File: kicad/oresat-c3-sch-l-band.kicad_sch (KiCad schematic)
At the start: 82 parts, among them U15 Qorvo 856930, U16 AX5043, U17 SI4112, U2 BP0805A1308, U29 TQP3M9036, U3 BP0805A1308, U4 BGB741L7ESD, U5 BP0805A1308, U7 MAC-24+

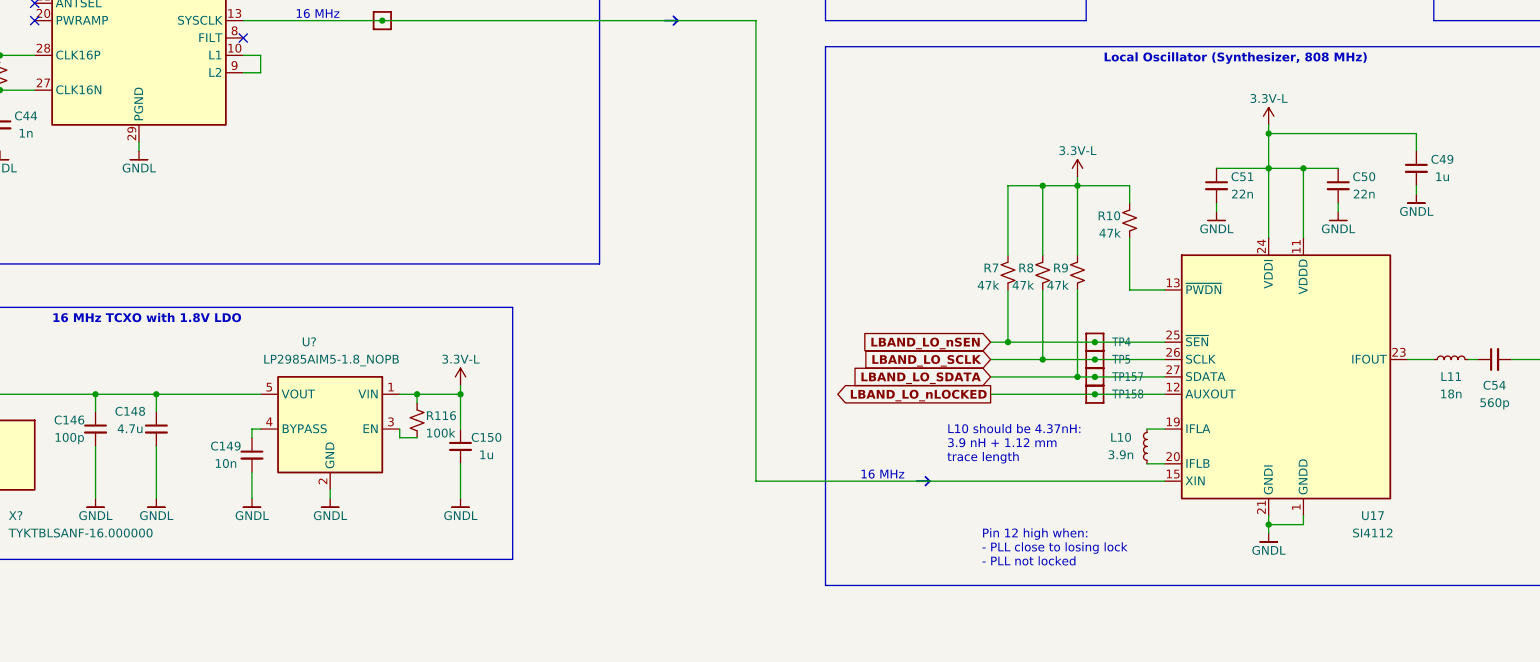
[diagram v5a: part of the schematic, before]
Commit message: More progress on C3 v6. All ICs and Packages are in, deployer and power supply and I2C subsystems laid out.
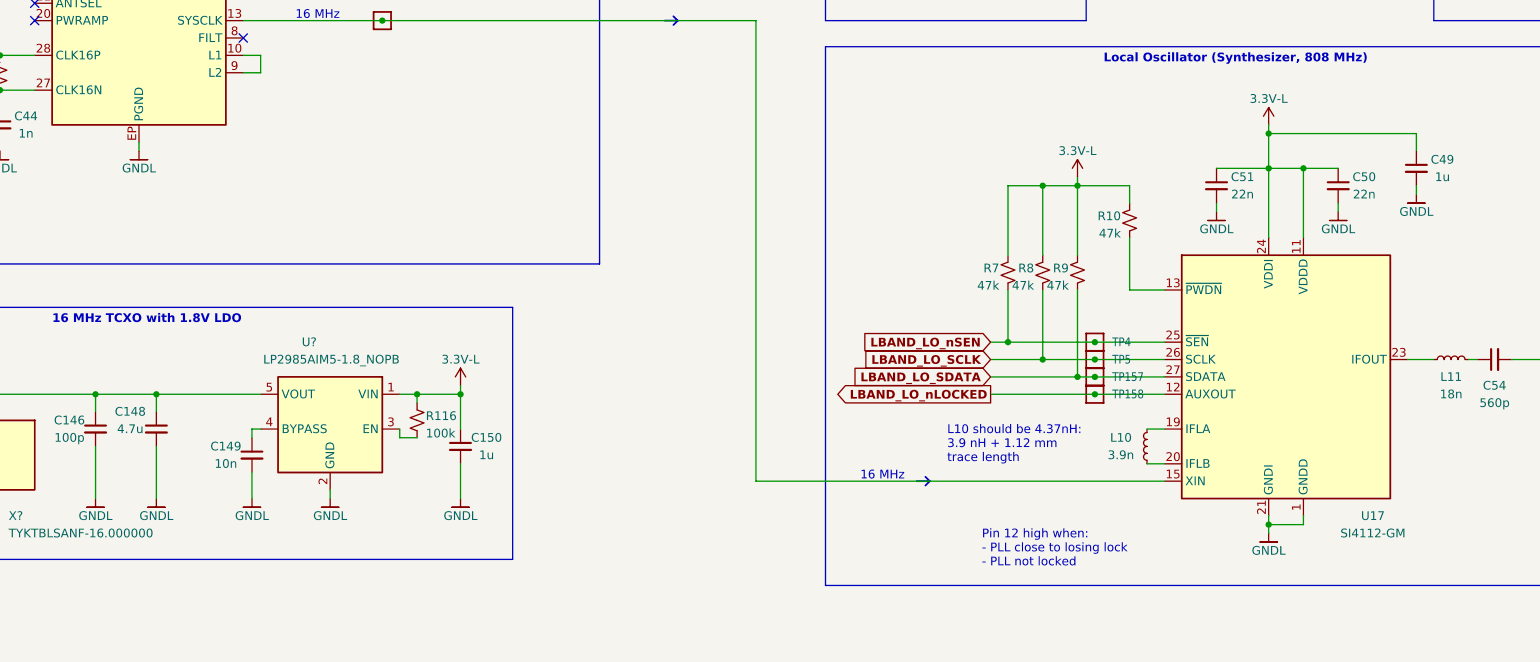
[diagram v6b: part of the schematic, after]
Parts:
- U15: footprint (none) -> oresat-ics:856930-saw-filter
- U16: footprint (none) -> oresat-ics:U-AX5043-QFN28-5X5-WITH-CENTER-PAD
- U17: value SI4112 -> SI4112-GM; footprint (none) -> Package_DFN_QFN:QFN-28-1EP_5x5mm_P0.5mm_EP3.35x3.35mm_ThermalVias
- U2, U3, U5: footprint (none) -> oresat-ics:BP0805
- U4: footprint (none) -> oresat-ics:Infineon-PG-TSLP-7-LNA
- U7: footprint (none) -> oresat-ics:MAC-24+
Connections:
- net GND: now also U16.EP (PGND), U17.29 (GNDD); no longer U16.29 (PGND), U4.10 (GND), U4.11 (GND), U4.12 (GND), U4.13 (GND), U4.14 (GND), U4.15 (GND), U4.8 (GND), U4.9 (GND)

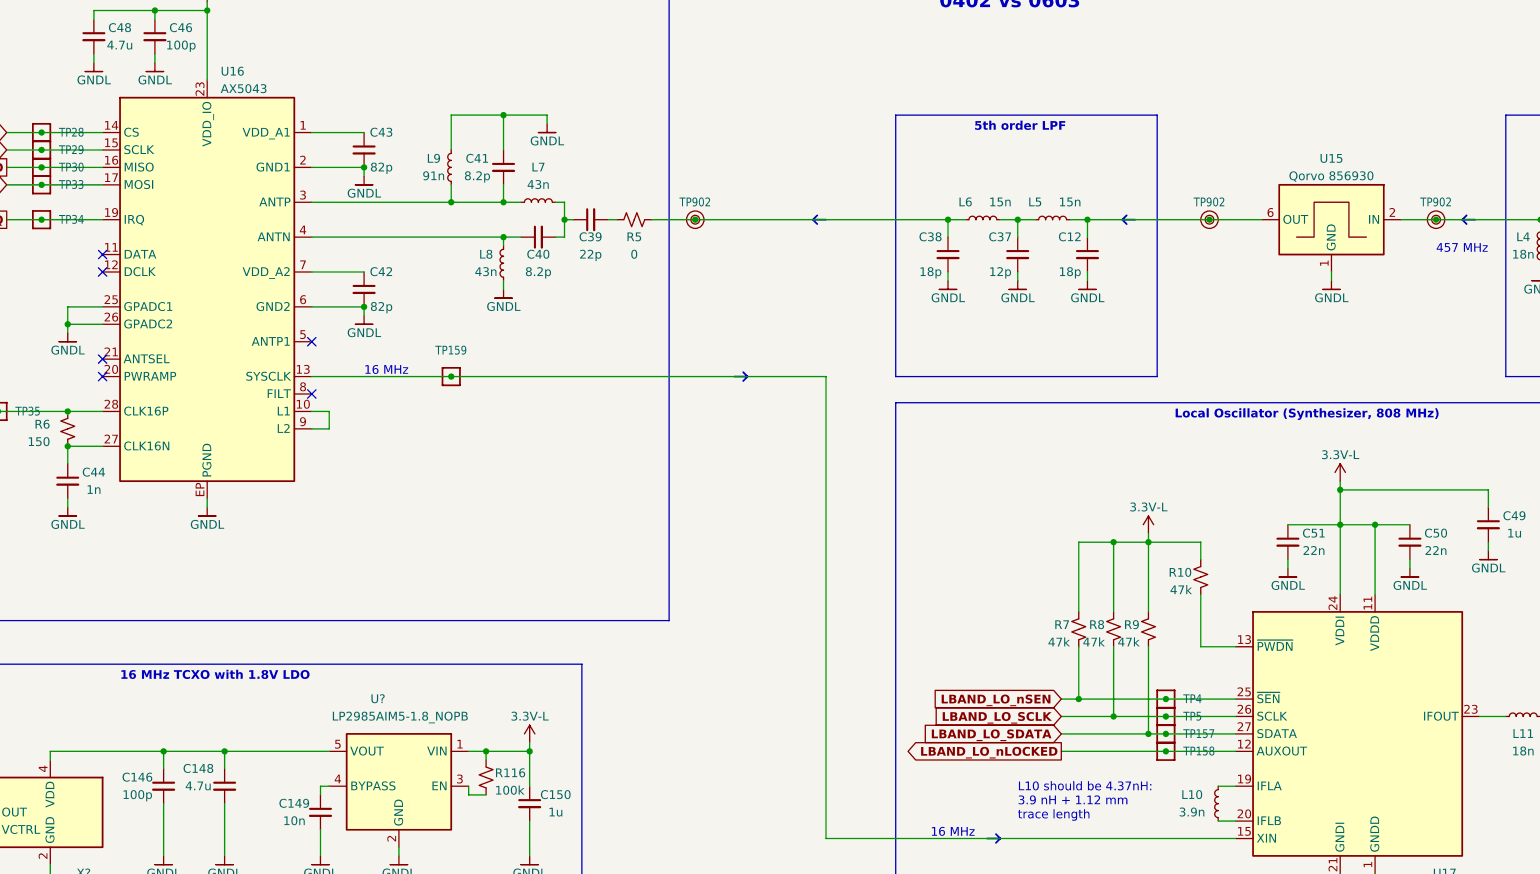
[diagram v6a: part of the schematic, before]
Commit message: routed everything but some minor lines and the radios. About to move the octavo and EVERYTHING else, wish me luck. Should give enough room for the radios!
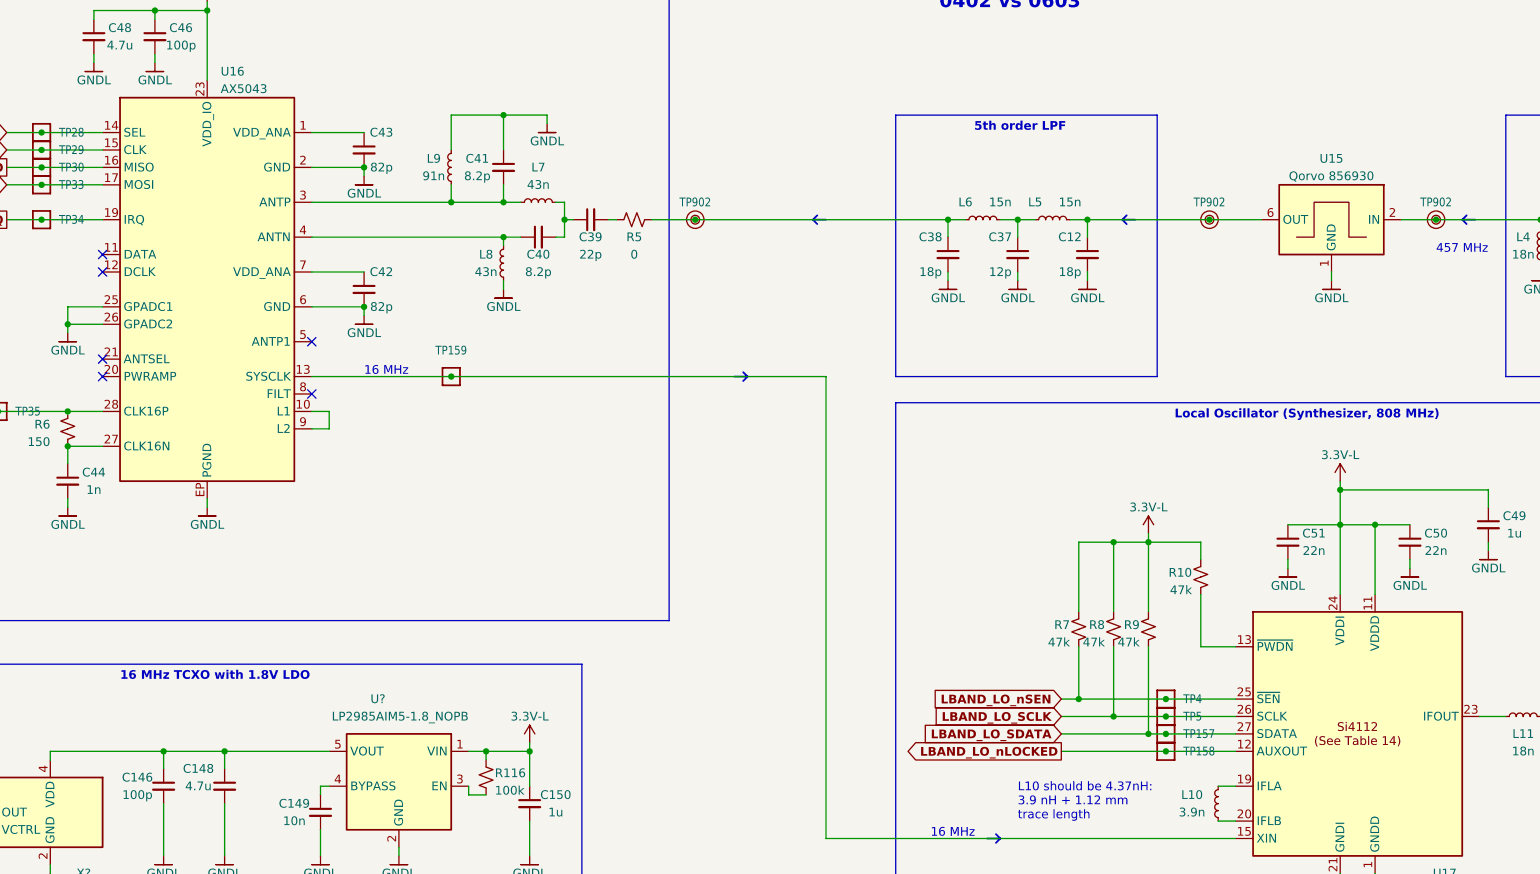
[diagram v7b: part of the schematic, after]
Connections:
- net GND: now also U17.16 (GNDD)
- net at U29.1 (NC), U29.3 (NC), U29.4 (NC)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: now also U29.5 (NC)
- new net: U16.18 (NC), U16.22 (NC), U16.24 (NC)
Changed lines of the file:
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@@
     (pin "14")
     (pin "15")
+    (pin "16")
     (pin "17")
     (pin "18")
@@
       (effects (font (size 1.27 1.27)) hide)
     )
-    (property "Datasheet" "" (at 119.38 121.92 0)
-      (effects (font (size 1.27 1.27)) hide)
-    )
+    (property "Datasheet" "https://www.mouser.com/datasheet/2/308/AX5043-D-782042.pdf" (at 119.38 121.92 0)
+      (effects (font (size 1.27 1.27)) hide)
+    )
+    (pin "18")
+    (pin "22")
+    (pin "24")
     (pin "1")
     (pin "10")
@@
       (effects (font (size 1.27 1.27)) hide)
     )
-    (pin "1")
-    (pin "2")
+    (pin "5")
+    (pin "1")
+    (pin "2")

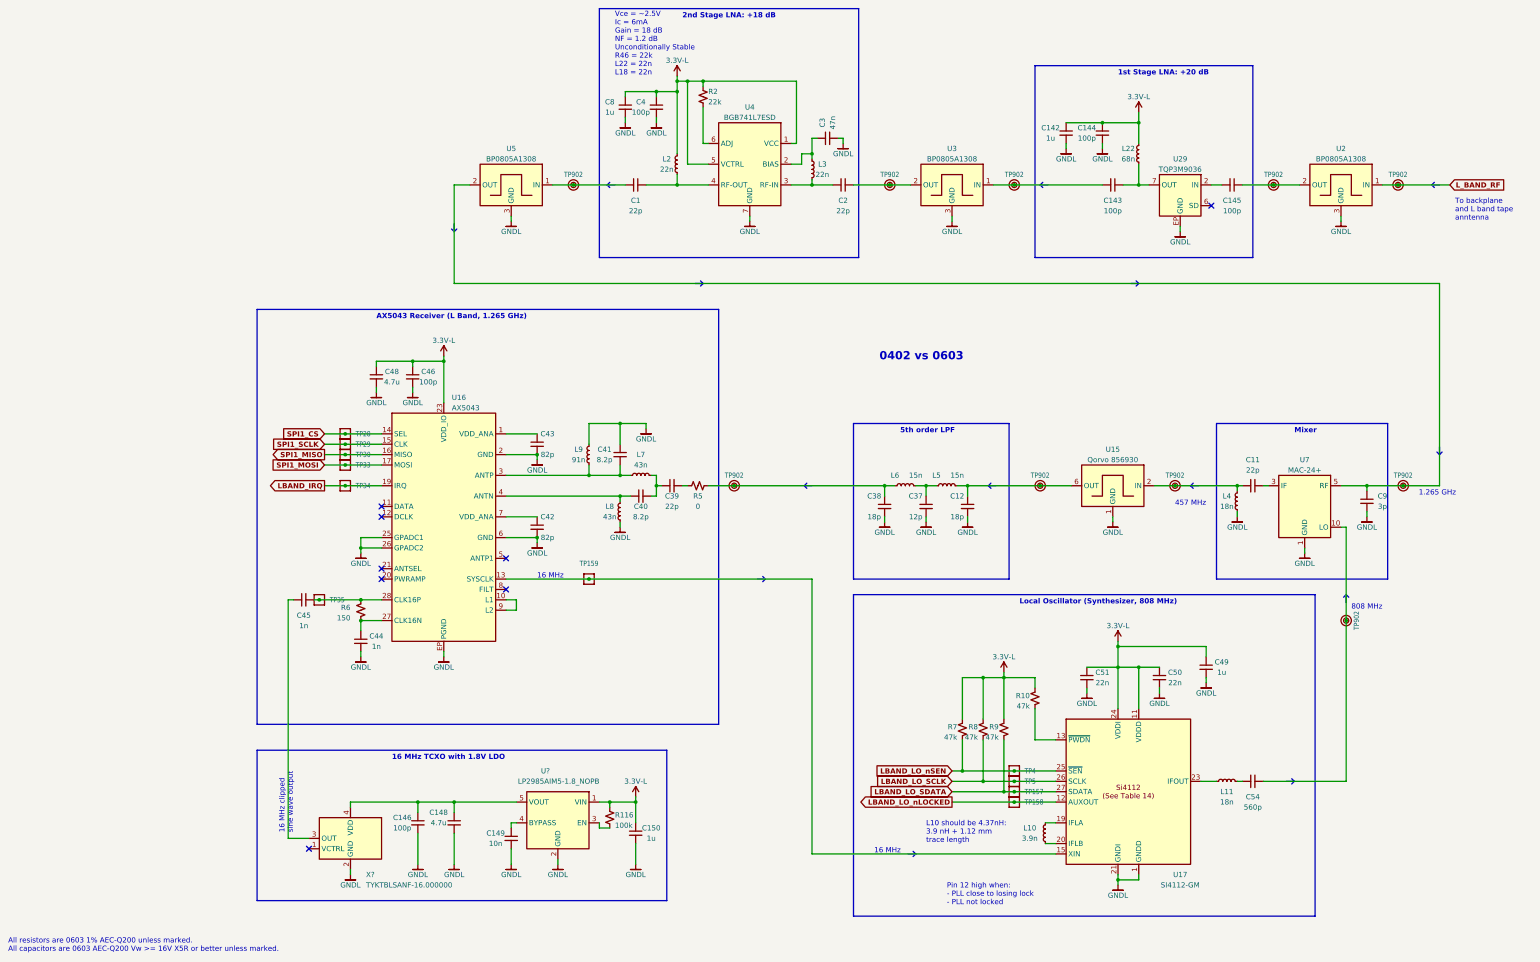
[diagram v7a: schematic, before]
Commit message: Switched all grounds to a single ground, because I can't find a way to overlap ground planes in KiCAD. That's actually not terrible, however, because KiCAD has an anti-plane feature which I used to cut the ground plane between UHF and L radios and L radio and Octavo. So actually I think it came out better than having separate ground planes. Only thing left now are the ~ 40 connections to the Octavo.
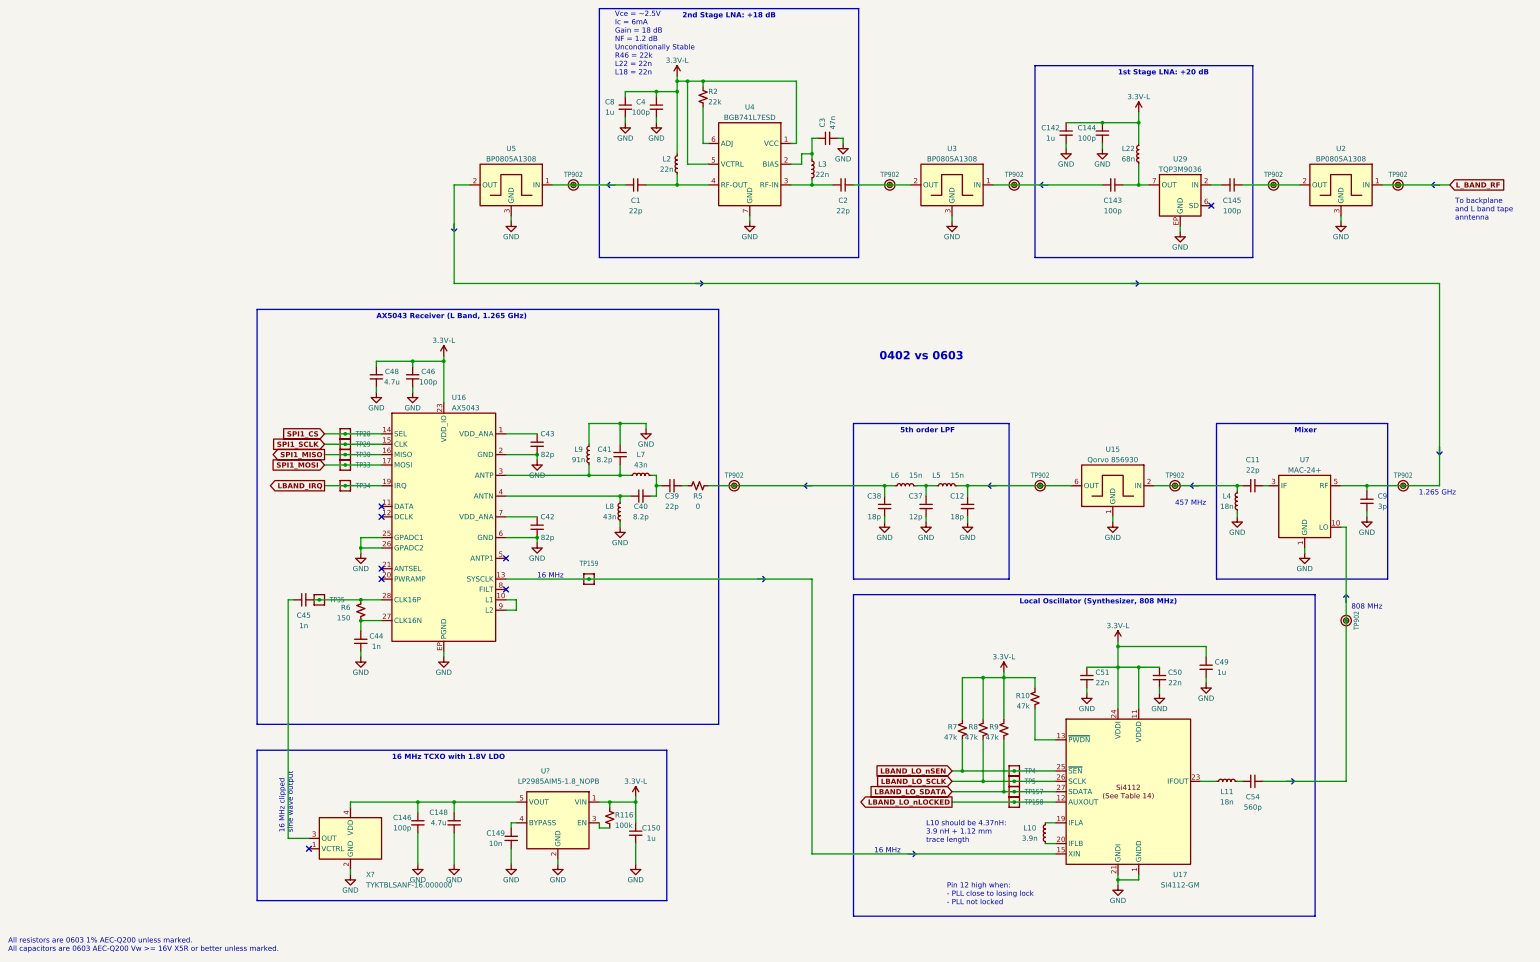
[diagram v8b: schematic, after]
